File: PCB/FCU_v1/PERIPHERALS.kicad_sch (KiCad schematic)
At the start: 62 parts, among them J11 USB_C_Receptacle_USB2.0_16P, J4 Conn_Coaxial_Small, U10 SN65HVD232, U3 TLV75533PDYDR, U4 BMI088, U5 LIS2MDL, U6 LPS22HH, U7 W25Q64JV, U8 USBLC6-2SC6, U9 MAX-M10M-20B

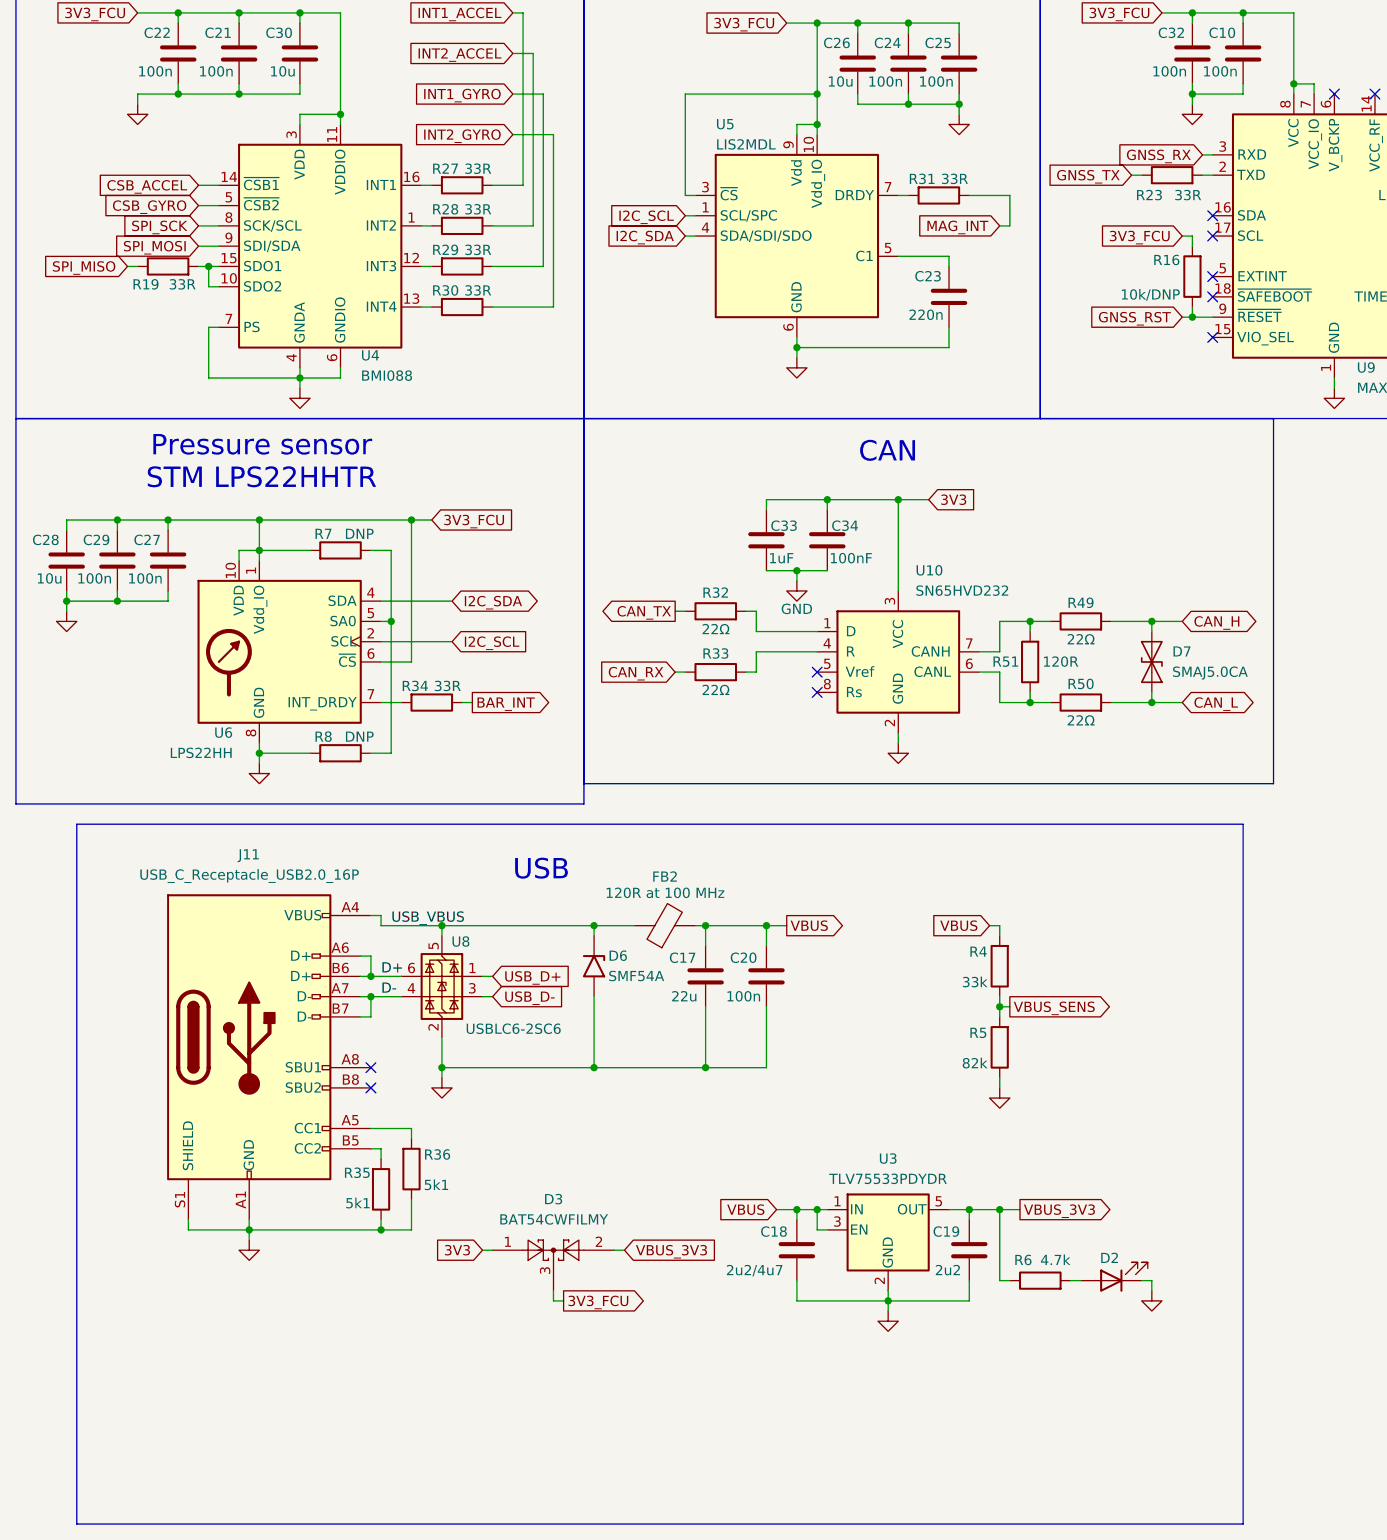
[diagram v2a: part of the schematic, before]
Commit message: Added next version v2
Added notes for next version with what needs to be improved or completely fixed. Notes in schematic file
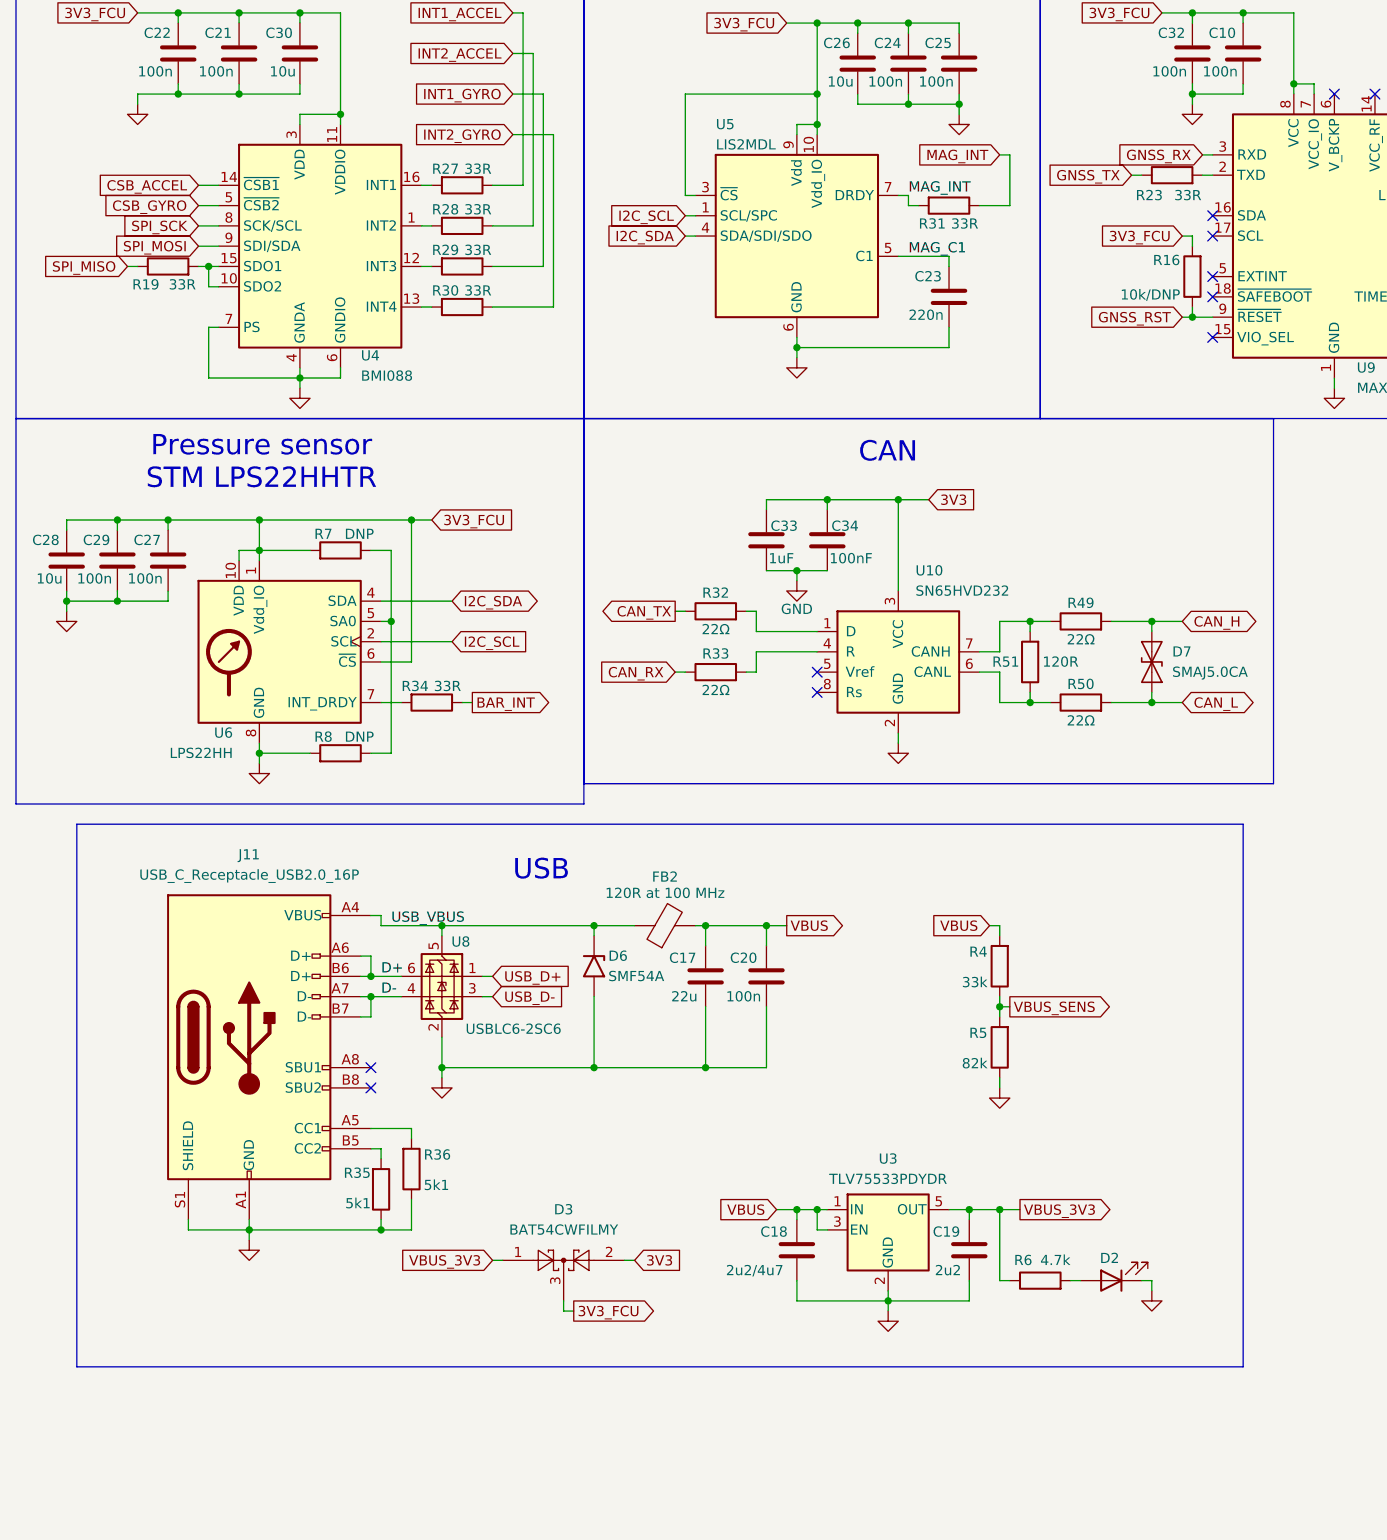
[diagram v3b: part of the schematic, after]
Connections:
- net 3V3: now also D3.2; no longer D3.1
- net MAG_INT: now also R31.2, U5.7 (DRDY)
- net VBUS_3V3: now also D3.1; no longer D3.2
- net MAG_C1: now reaches C23.1, U5.5 (C1)
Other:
- moved on the sheet: D3, R31
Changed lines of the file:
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@@
 	(rectangle
 		(start 24.13 128.27)
-		(end 170.18 215.9)
+		(end 170.18 196.215)
 		(stroke
 			(width 0)
@@
 	(wire
 		(pts
-			(xy 127 49.53) (xy 128.27 49.53)
-		)
-		(stroke
-			(width 0)
-			(type default)
-		)
-	)
-	(wire
-		(pts
 			(xy 143.51 113.03) (xy 146.05 113.03)
 		)
@@
 	(wire
 		(pts
-			(xy 91.44 181.61) (xy 92.71 181.61)
+			(xy 92.71 182.88) (xy 93.98 182.88)
 		)
 		(stroke
@@
 	(wire
 		(pts
-			(xy 140.97 49.53) (xy 140.97 53.34)
+			(xy 143.51 102.87) (xy 146.05 102.87)
 		)
 		(stroke
@@
 	(wire
 		(pts
-			(xy 143.51 102.87) (xy 146.05 102.87)
+			(xy 46.99 93.98) (xy 53.34 93.98)
 		)
 		(stroke
@@
 	(wire
 		(pts
-			(xy 46.99 93.98) (xy 53.34 93.98)
+			(xy 68.58 48.26) (xy 67.31 48.26)
 		)
 		(stroke
@@
 	(wire
 		(pts
-			(xy 68.58 48.26) (xy 67.31 48.26)
+			(xy 76.2 149.86) (xy 74.93 149.86)
 		)
 		(stroke
@@
 	(wire
 		(pts
-			(xy 76.2 149.86) (xy 74.93 149.86)
+			(xy 128.27 50.8) (xy 129.54 50.8)
 		)
 		(stroke
@@
 	(wire
 		(pts
-			(xy 139.7 53.34) (xy 140.97 53.34)
-		)
-		(stroke
-			(width 0)
-			(type default)
-		)
-	)
-	(wire
-		(pts
 			(xy 39.37 50.8) (xy 41.91 50.8)
 		)
@@
 	(wire
 		(pts
+			(xy 140.97 50.8) (xy 140.97 44.45)
+		)
+		(stroke
+			(width 0)
+			(type default)
+		)
+	)
+	(wire
+		(pts
 			(xy 139.7 149.86) (xy 139.7 151.13)
 		)
@@
 	(wire
 		(pts
+			(xy 128.27 49.53) (xy 128.27 50.8)
+		)
+		(stroke
+			(width 0)
+			(type default)
+		)
+	)
+	(wire
+		(pts
 			(xy 78.74 26.67) (xy 80.01 26.67)
 		)
@@
 	(wire
 		(pts
+			(xy 137.16 50.8) (xy 140.97 50.8)
+		)
+		(stroke
+			(width 0)
+			(type default)
+		)
+	)
+	(wire
+		(pts
 			(xy 116.84 27.94) (xy 121.92 27.94)
 		)
@@
 	(wire
 		(pts
-			(xy 74.93 181.61) (xy 76.2 181.61)
+			(xy 76.2 182.88) (xy 77.47 182.88)
 		)
 		(stroke
@@
 	(wire
 		(pts
-			(xy 135.89 49.53) (xy 140.97 49.53)
-		)
-		(stroke
-			(width 0)
-			(type default)
-		)
-	)
-	(wire
-		(pts
 			(xy 170.18 35.56) (xy 170.18 36.83)
 		)
@@
 	(wire
 		(pts
-			(xy 83.82 187.96) (xy 85.09 187.96)
+			(xy 85.09 189.23) (xy 86.36 189.23)
 		)
 		(stroke
@@
 	(wire
 		(pts
-			(xy 83.82 186.69) (xy 83.82 187.96)
+			(xy 85.09 187.96) (xy 85.09 189.23)
 		)
 		(stroke
@@
 	(wire
 		(pts
+			(xy 140.97 44.45) (xy 139.7 44.45)
+		)
+		(stroke
+			(width 0)
+			(type default)
+		)
+	)
+	(wire
+		(pts
 			(xy 127 87.63) (xy 127 99.06)
 		)
@@
 	(wire
 		(pts
+			(xy 127 49.53) (xy 128.27 49.53)
+		)
+		(stroke
+			(width 0)
+			(type default)
+		)
+	)
+	(wire
+		(pts
 			(xy 82.55 36.83) (xy 78.74 36.83)
 		)
@@
 		)
 	)
+	(label "MAG_C1"
+		(at 128.27 57.15 0)
+		(effects
+			(font
+				(size 1.27 1.27)
+			)
+			(justify left bottom)
+		)
+	)
 	(label "D+"
 		(at 62.23 147.32 0)
@@
 		)
 	)
+	(label "MAG_INT"
+		(at 128.27 49.53 0)
+		(effects
+			(font
+				(size 1.27 1.27)
+			)
+			(justify left bottom)
+		)
+	)
 	(label "D-"
 		(at 62.23 149.86 0)
@@
 		)
 	)
+	(global_label "3V3"
+		(shape input)
+		(at 93.98 182.88 0)
+		(fields_autoplaced yes)
+		(effects
+			(font
+				(size 1.27 1.27)
+			)
+			(justify left)
+		)
+		(property "Intersheetrefs" "${INTERSHEET_REFS}"
+			(at 100.4728 182.88 0)
+			(effects
+				(font
+					(size 1.27 1.27)
+				)
+				(justify left)
+				(hide yes)
+			)
+		)
+	)
 	(global_label "I2C_SDA"
 		(shape bidirectional)
@@
 	(global_label "3V3_FCU"
 		(shape output)
-		(at 85.09 187.96 0)
+		(at 86.36 189.23 0)
 		(fields_autoplaced yes)
 		(effects
@@
 		)
 		(property "Intersheetrefs" "${INTERSHEET_REFS}"
-			(at 96.2395 187.96 0)
+			(at 97.5095 189.23 0)
 			(effects
 				(font
@@
 		)
 	)
-	(global_label "VBUS_3V3"
-		(shape input)
-		(at 92.71 181.61 0)
-		(fields_autoplaced yes)
-		(effects
-			(font
-				(size 1.27 1.27)
-			)
-			(justify left)
-		)
-		(property "Intersheetrefs" "${INTERSHEET_REFS}"
-			(at 105.069 181.61 0)
-			(effects
-				(font
-					(size 1.27 1.27)
-				)
-				(justify left)
-				(hide yes)
-			)
-		)
-	)
 	(global_label "3V3_FCU"
 		(shape input)
@@
 		)
 	)
-	(global_label "3V3"
-		(shape input)
-		(at 74.93 181.61 180)
-		(fields_autoplaced yes)
-		(effects
-			(font
-				(size 1.27 1.27)
-			)
-			(justify right)
-		)
-		(property "Intersheetrefs" "${INTERSHEET_REFS}"
-			(at 68.4372 181.61 0)
-			(effects
-				(font
-					(size 1.27 1.27)
-				)
-				(justify right)
-				(hide yes)
-			)
-		)
-	)
 	(global_label "VBUS"
 		(shape input)
@@
 	(global_label "MAG_INT"
 		(shape input)
-		(at 139.7 53.34 180)
+		(at 139.7 44.45 180)
 		(fields_autoplaced yes)
 		(effects
@@
 		)
 		(property "Intersheetrefs" "${INTERSHEET_REFS}"
-			(at 129.0343 53.34 0)
+			(at 129.0343 44.45 0)
 			(effects
 				(font
@@
 		)
 	)
+	(global_label "VBUS_3V3"
+		(shape input)
+		(at 76.2 182.88 180)
+		(fields_autoplaced yes)
+		(effects
+			(font
+				(size 1.27 1.27)
+			)
+			(justify right)
+		)
+		(property "Intersheetrefs" "${INTERSHEET_REFS}"
+			(at 63.841 182.88 0)
+			(effects
+				(font
+					(size 1.27 1.27)
+				)
+				(justify right)
+				(hide yes)
+			)
+		)
+	)
 	(global_label "SPI_SCK"
 		(shape input)
@@
 	(symbol
 		(lib_id "Device:R")
-		(at 132.08 49.53 270)
+		(at 133.35 50.8 270)
 		(unit 1)
 		(exclude_from_sim no)
@@
 		(dnp no)
 		(property "Reference" "R31"
-			(at 128.27 47.498 90)
+			(at 129.54 53.086 90)
 			(effects
 				(font
@@
 		)
 		(property "Value" "33R"
-			(at 132.334 47.498 90)
+			(at 133.604 53.086 90)
 			(effects
 				(font
@@
 		)
 		(property "Footprint" "Resistor_SMD:R_0603_1608Metric"
-			(at 132.08 47.752 90)
+			(at 133.35 49.022 90)
 			(effects
 				(font
@@
 		)
 		(property "Datasheet" "~"
-			(at 132.08 49.53 0)
+			(at 133.35 50.8 0)
 			(effects
 				(font
@@
 		)
 		(property "Description" "Resistor"
-			(at 132.08 49.53 0)
+			(at 133.35 50.8 0)
 			(effects
 				(font
@@
 	(symbol
 		(lib_id "Diode:BAT54CW")
-		(at 83.82 181.61 0)
+		(at 85.09 182.88 0)
 		(unit 1)
 		(exclude_from_sim no)
@@
 		(fields_autoplaced yes)
 		(property "Reference" "D3"
-			(at 83.82 175.26 0)
+			(at 85.09 176.53 0)
 			(effects
 				(font
@@
 		)
 		(property "Value" "BAT54CWFILMY"
-			(at 83.82 177.8 0)
+			(at 85.09 179.07 0)
 			(effects
 				(font
@@
 		)
 		(property "Footprint" "Package_TO_SOT_SMD:SOT-323_SC-70"
-			(at 85.725 178.435 0)
+			(at 86.995 179.705 0)
 			(effects
 				(font
@@
 		)
 		(property "Datasheet" "https://assets.nexperia.com/documents/data-sheet/BAT54W_SER.pdf"
-			(at 81.788 181.61 0)
+			(at 83.058 182.88 0)
 			(effects
 				(font
@@
 		)
 		(property "Description" "Dual schottky barrier diode, common cathode, SOT-323"
-			(at 83.82 181.61 0)
+			(at 85.09 182.88 0)
 			(effects
 				(font

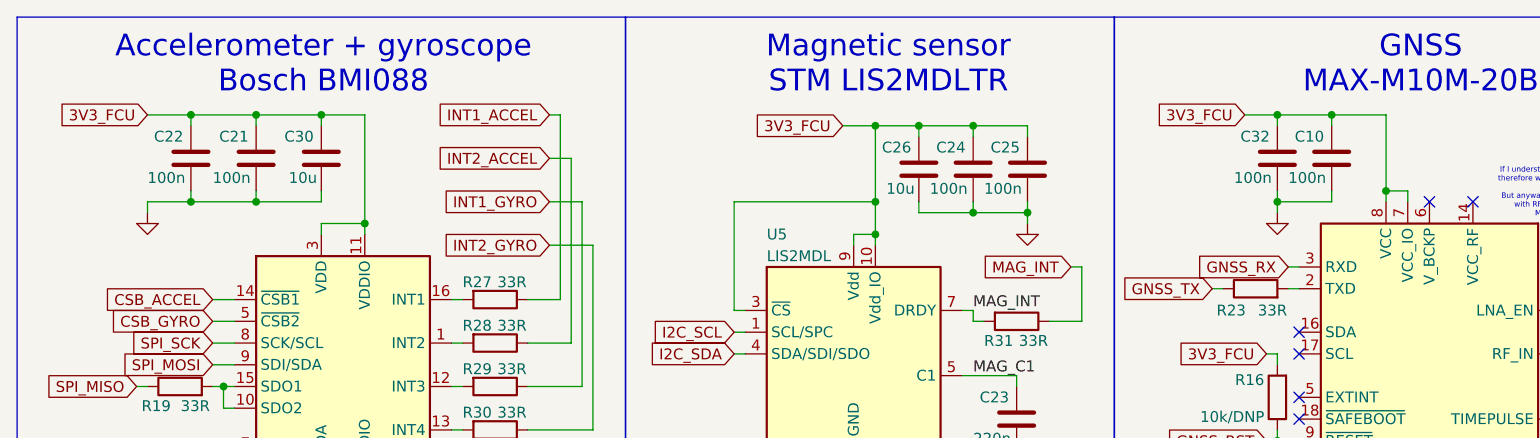
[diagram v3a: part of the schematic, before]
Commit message: Update PCB footprints, positions and backups
Remove old FCU_v1 backup zips and add new timestamped backups. Apply extensive edits to PCB/FCU_v1.kicad_pcb: reposition and rotate multiple footprints, fix pad orientations, update silkscreen/fab/crtyd outlines and UUIDs, change some net mappings and sheet/path references, and replace a resistor footprint with a SOT-23-6 ESD device (USBLC6) including updated properties and datasheet. Update related project/schematic files (FCU_v1.kicad_prl, FCU_v1.kicad_sch, PERIPHERALS.kicad_sch) to reflect these changes.
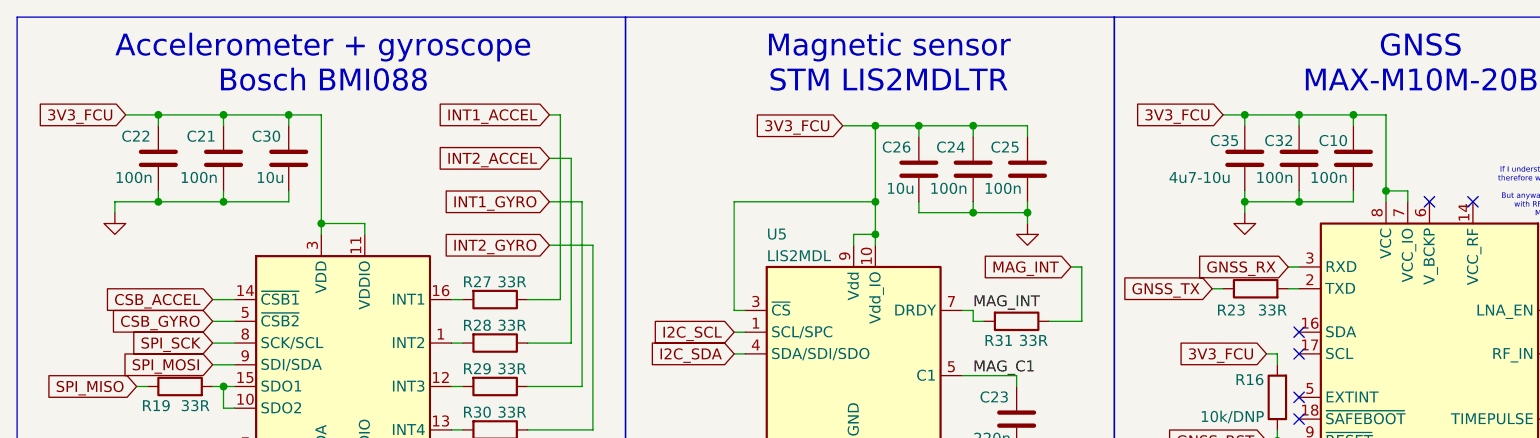
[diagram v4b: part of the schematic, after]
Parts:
- added C35: 4u7-10u, Capacitor_SMD:C_0805_2012Metric, symbol Device:C
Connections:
- net 3V3_FCU: now also C35.1
- net GND: now also C35.2
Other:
- moved on the sheet: C10, C21, C22, C30, C32

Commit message: Layout update
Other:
- moved on the sheet: C10, C32, C35, D4, J4, R15, R16, R23, U9
